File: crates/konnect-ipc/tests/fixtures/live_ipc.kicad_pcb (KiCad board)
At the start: 2 copper layers, 160 x 100 mm, 4 parts

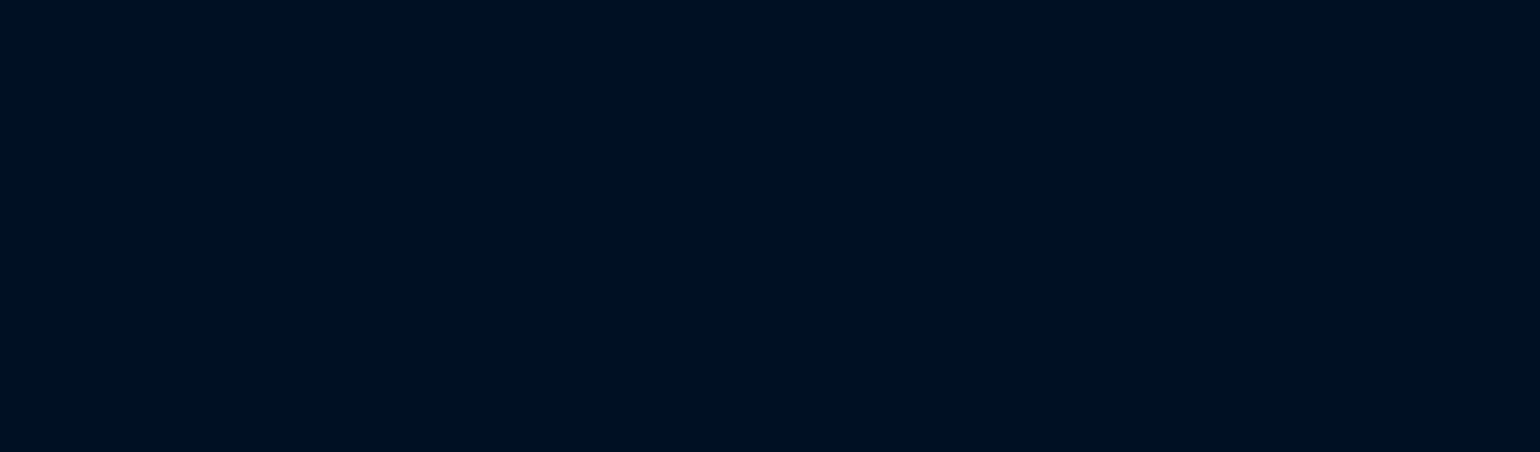
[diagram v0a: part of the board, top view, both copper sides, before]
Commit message: test(live): give the live fixture nets, and guard its preconditions
Josh ran the live suite against KiCad 10.0.4 on macOS. The move/rotate
test PASSED — the first time anything in this file has been confirmed to
run. The other two never reached the code under test:

    board has no named net to attach a via to   (live_kicad_test.rs:179)
    board has no named net to attach a zone to  (live_kicad_test.rs:245)

`fixtures/live_ipc.kicad_pcb` is the stock EuroCard template, and its
net table declares only the unnamed net 0. With no named net `get_nets`
returns nothing usable and both net-attached tests die on their own
`expect`. The pre-existing `add_via` test therefore could never have
passed against this fixture in any environment — independent evidence
that the live suite has never actually run anywhere.

* The fixture gains `GND` and `SIG1`, in the legacy table-and-id shape
  the board already uses. An 18-line pure addition; no format churn.
* Both tests' coordinates move inside the board. The template is not at
  the origin — its outline is (55, 45) to (215, 145) — so the via test's
  (40, 40) was off the board entirely, and the zone test's outline,
  which I wrote, was half off it. The via spot is now (100, 120) and the
  zone outline (150, 95)-(190, 115), clear of the guide-rail keepouts.
* The zone outline straddles the GND segment on purpose. `add_zone` sets
  island removal to `IRM_ALWAYS`, KiCad's default, so a pour reaching
  nothing else on its own net has its whole fill discarded as islands —
  the `filled_polygons` assertion would have failed on a floating zone
  even once a net existed. The test asks for GND by name rather than
  taking whichever net comes back first.
* New `the_live_fixture_satisfies_what_the_live_tests_assume`, which is
  deliberately NOT `#[ignore]`d: the fixture still has GND plus a second
  named net, is still in its expected net shape, both tests' coordinates
  lie inside the Edge.Cuts outline, and a GND segment crosses the zone
 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
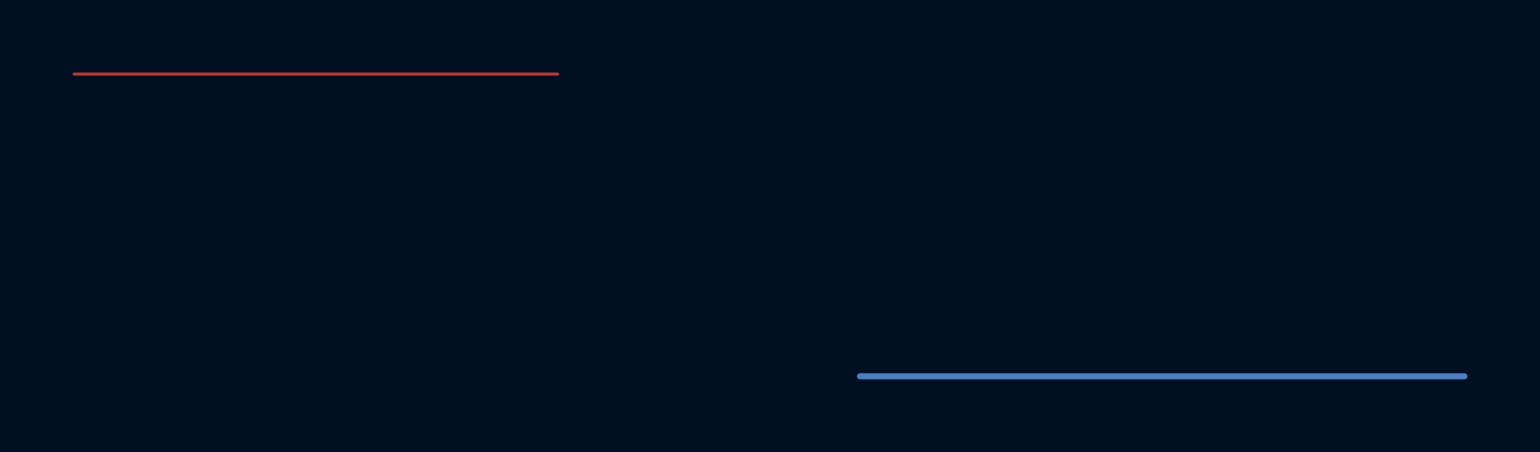
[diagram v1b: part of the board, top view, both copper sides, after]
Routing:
- net GND: track 0.00 -> 50.0 mm
- net SIG1: track 0.00 -> 40.0 mm
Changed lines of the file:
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@@
 	)
 	(net 0 "")
+	(net 1 "GND")
+	(net 2 "SIG1")
 	(footprint "MountingHole:MountingHole_2.7mm_M2.5_DIN965"
 		(locked yes)
@@
 		)
 	)
+	(segment
+		(start 145 105)
+		(end 195 105)
+		(width 0.5)
+		(layer "B.Cu")
+		(net 1)
+	)
+	(segment
+		(start 80 80)
+		(end 120 80)
+		(width 0.25)
+		(layer "F.Cu")
+		(net 2)
+	)
 	(embedded_fonts no)
